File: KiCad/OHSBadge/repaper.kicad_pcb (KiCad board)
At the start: 2 copper layers, 101.6 x 50.8 mm, 59 parts, among them J1 HEADER1X10MS2.54, J2 HEADER1X10MS2.54, J4 ZIF-40-0.5, P1 PCB, Q1 AP2305, Q2 2N7002KW, Q3 BSS84W, Q4 2N7002KW, Q5 2N7002KW, Q6 2N7002KW, Q7 BSS84W, SW1 SEL, SW2 UP, SW3 DOWN, U1 MCP9700AT-E/TT, U3 TPS77030, U4 TXS0108

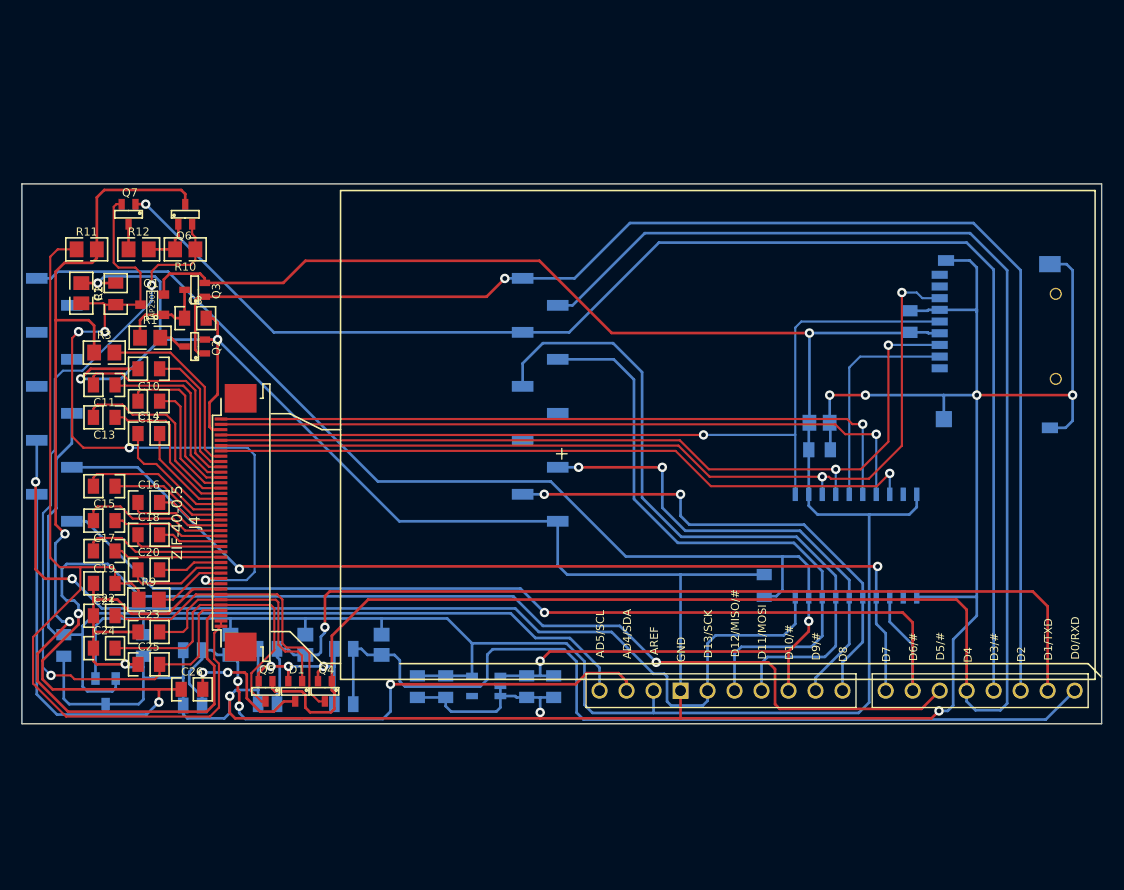
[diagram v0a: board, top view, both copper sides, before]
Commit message: OHSBadge : added 328P, and full Arduino shield. See Board outline for lanyard looping option.
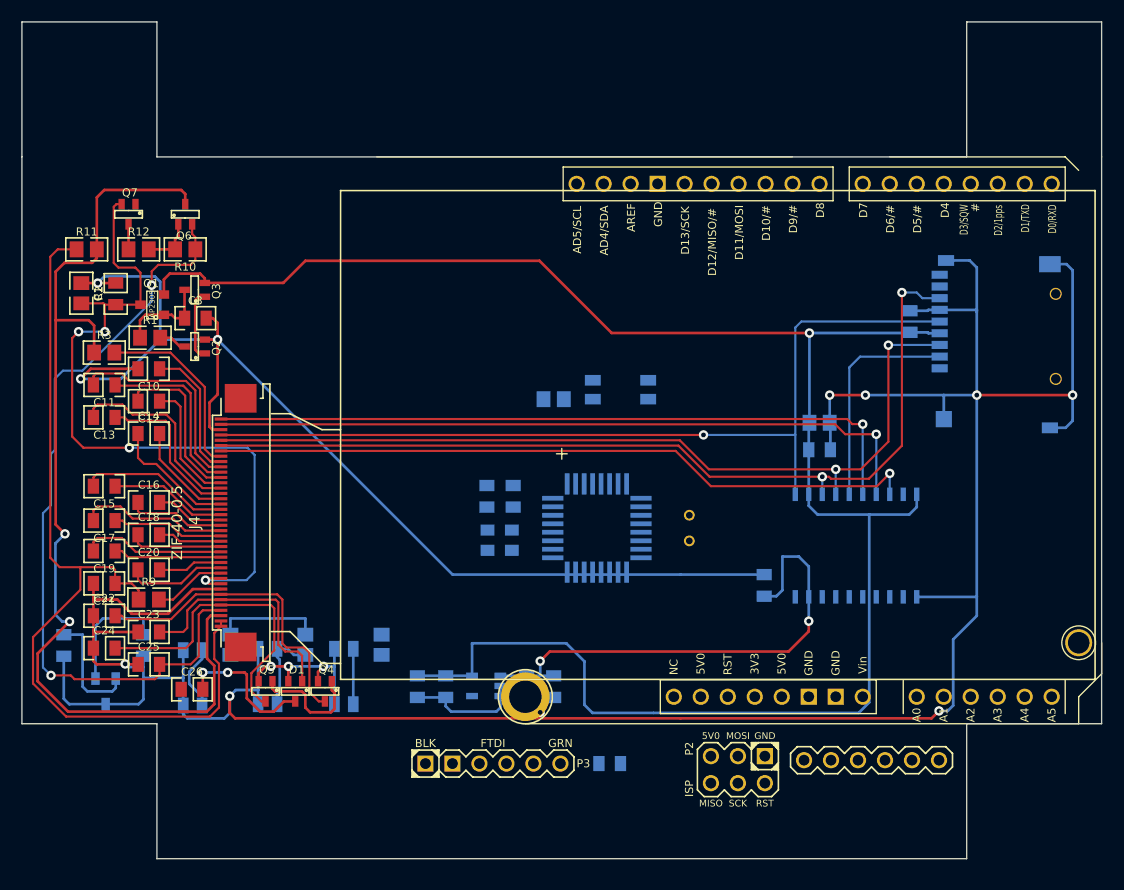
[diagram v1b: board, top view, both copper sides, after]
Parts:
- removed J1, J2: HEADER1X10MS2.54, Sck-10-F-SMT
- added B1: I/O, I/O, F.Cu at (88.2, 84.4)
- added B2: I/O, I/O, F.Cu at (88.2, 82.0)
- added C31: 0.1u,16V, c_0805, B.Cu at (80.7, 105.3)
- added C6: 22pF, c_0805, B.Cu at (71.6, 80.2)
- added C9: 22pF, c_0805, B.Cu at (69.2, 80.2)
- added P2: ISP, Header_ISP, F.Cu at (92.8, 105.9)
- added P3: FTDI, Header_FTDI, F.Cu at (69.7, 105.3)
- added P4: C3SB, Header_6x1, F.Cu at (105.3, 105.0)
- added R7: 10k, r_0805, B.Cu at (75.4, 71.1)
- added SW4: RST, SW_SMD, B.Cu at (81.7, 70.2)
- added U2: ATMEGA328-AU-ND, TQFP32, B.Cu at (79.5, 83.2)
- added X1: CRYSTAL_16MHz, Xtal_SMD2, B.Cu at (70.4, 84.3)
- SHIELD1: footprint ARDUINO_BUCKLER -> ARDUINO_SHIELD_2_040pins
- moved SHIELD1 65.9 mm to (58.8, 101.6)
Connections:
- R4 pad 1: /SDA -> N-0000034
- R4 pad 2: +3.3V -> /VCC5V
- R5 pad 1: /TXD -> N-0000035
- R5 pad 2: +3.3V -> /VCC5V
- R6 pad 1: /RXD -> N-0000036
- R6 pad 2: +3.3V -> /VCC5V
- SHIELD1 pad 10: /VCC5V -> (no net)
- SHIELD1 pad 2: /PANEL_ON -> (no net)
- SHIELD1 pad 3: /BORDER_CONTROL -> (no net)
- SHIELD1 pad 4: /DISCHARGE -> (no net)
- SHIELD1 pad 5: /PWM -> (no net)
- SHIELD1 pad 6: //RESET -> (no net)
- SHIELD1 pad 7: /BUSY -> (no net)
- SHIELD1 pad 8: //EPD_CS -> (no net)
- SHIELD1 pad 9: /FLASH_CS -> (no net)
- SHIELD1 pad AD4: /SDA -> /SCL
- SHIELD1 pad AD5: /TEMPERATURE -> /SCL
- SW1 pad 1: /SDA -> N-0000036
- SW2 pad 1: /TXD -> N-0000035
- SW3 pad 1: /RXD -> N-0000034
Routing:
- net /DISCHARGE: track 177.2 -> 11.0 mm
- net /PWM: track 150.2 -> 0.00 mm, vias 3 -> 0
- net /BORDER_CONTROL: track 129.9 -> 0.00 mm, vias 1 -> 0
- net /PANEL_ON: track 127.8 -> 6.74 mm, vias 1 -> 0
- net /SPI_CLK: track 99.2 -> 0.00 mm, vias 2 -> 0
- net //RESET: track 99.2 -> 0.00 mm, vias 1 -> 0
- net /TXD: track 92.0 -> 0.00 mm, vias 1 -> 0
- net /BUSY: track 92.0 -> 0.00 mm, vias 2 -> 0
- net /RXD: track 85.2 -> 0.00 mm
- net /TEMPERATURE: track 88.0 -> 11.0 mm
- net /VCC5V: track 132.1 -> 57.0 mm
- net /SPI_MOSI: track 65.3 -> 0.00 mm
- net /SPI_MISO: track 58.3 -> 0.00 mm
- net /SDA: track 56.0 -> 0.00 mm, vias 3 -> 0
- net //EPD_CS: track 47.6 -> 0.00 mm, vias 2 -> 0
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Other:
- board size 101.6 x 50.8 mm -> 101.6 x 78.7 mm

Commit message: OHSBadge, work in progress
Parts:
- added H1: I/O, vite_3mm, F.Cu at (31.8, 41.9)
- added H2: I/O, vite_3mm, F.Cu at (120.7, 41.9)
- P4: footprint Header_6x1 -> pin_strip_4-90
- moved P3 19.0 mm to (50.8, 106.7)
- moved C31 18.5 mm to (62.2, 106.6)
- moved P2 16.6 mm to (76.2, 105.4)
- moved P4 4.09 mm to (101.6, 106.7), turned to 0 degrees
- moved P1 1.27 mm to (76.2, 74.9)
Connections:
- SHIELD1 pad AD4: /SCL -> /SDA

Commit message: OHSBadge working on board layout.
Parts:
- added G***: LOGO, LOGO, F.Cu at (32.3, 56.6)
- added G***: LOGO, OSHW_6mm, F.Cu at (98.0, 110.2)
- added G***: LOGO, seeed_LOGO, F.Cu at (118.9, 63.9)
- added G1: Logo-WL3, Logo-WL3, F.Cu at (26.1, 93.6)
- C1, C10, C11, C12, C13, C14, C15, C16, C17, C18, C19, C20, C21, C22, C23, C24, C25, C26, C3, D1, P2, P3, P4, Q1, Q2, Q3, Q4, Q5, Q6, Q7, R1, R10, R11, R12, R2, R3, R9: moved to B.Cu
- J4: footprint ZIF-40-0.5 -> ZIF-40-0.5-M
- SW1: value SEL -> UP; moved to F.Cu
- SW2: value UP -> SEL; moved to F.Cu
- SW3, SW4: moved to F.Cu
- moved C8 64.1 mm to (89.2, 71.5), turned to 180 degrees
- moved U1 60.9 mm to (89.4, 74.9), turned to 90 degrees
- moved C7 54.7 mm to (89.2, 78.4), turned to 0 degrees
- moved R4 47.8 mm to (91.4, 105.7), turned to 90 degrees
- moved SW4 47.8 mm to (109.2, 109.2), turned to 90 degrees
- moved R7 45.0 mm to (104.1, 105.7), turned to 90 degrees
- moved P2 44.0 mm to (116.8, 88.6), turned to 90 degrees
- moved SW3 33.0 mm to (86.4, 109.2), turned to 90 degrees
- moved P4 32.7 mm to (118.1, 78.5), turned to 270 degrees
- moved R5 31.4 mm to (81.3, 105.7), turned to 90 degrees
- moved SW2 30.2 mm to (76.2, 109.2), turned to 90 degrees
- moved SW1 27.3 mm to (66.0, 109.2), turned to 90 degrees
- moved R3 21.6 mm to (54.7, 66.6), turned to 180 degrees
- moved C11 21.6 mm to (54.7, 69.7), turned to 0 degrees
- moved C13 21.6 mm to (54.7, 72.8), turned to 0 degrees
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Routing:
- net GND: track 394.1 -> 0.00 mm, vias 14 -> 0
- net +3.3V: track 187.4 -> 0.00 mm, vias 1 -> 0
- net /BORDER: track 95.5 -> 0.00 mm, vias 2 -> 0
- net /SPI_MISO_COG: track 86.5 -> 0.00 mm, vias 2 -> 0
- net /SPI_CLK_COG: track 83.6 -> 0.00 mm, vias 1 -> 0
- net /VCOM: track 82.8 -> 0.00 mm
- net /SPI_MOSI_COG: track 81.3 -> 0.00 mm, vias 2 -> 0
- net /VDL: track 73.4 -> 0.00 mm, vias 2 -> 0
- net /VCC_T: track 69.8 -> 0.00 mm, vias 4 -> 0
- net /BUSY_COG: track 67.7 -> 0.00 mm, vias 1 -> 0
- net /EPD_CS_COG: track 67.2 -> 0.00 mm, vias 1 -> 0
- net /RESET_COG: track 66.8 -> 0.00 mm, vias 1 -> 0
- net /VCC5V: track 57.0 -> 0.00 mm, vias 2 -> 0
- net /VGH: track 29.6 -> 0.00 mm
- net /VDH: track 28.8 -> 0.00 mm
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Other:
- outline, holes or cut-outs redrawn
- board text added: "SLOT FOR CABLE"

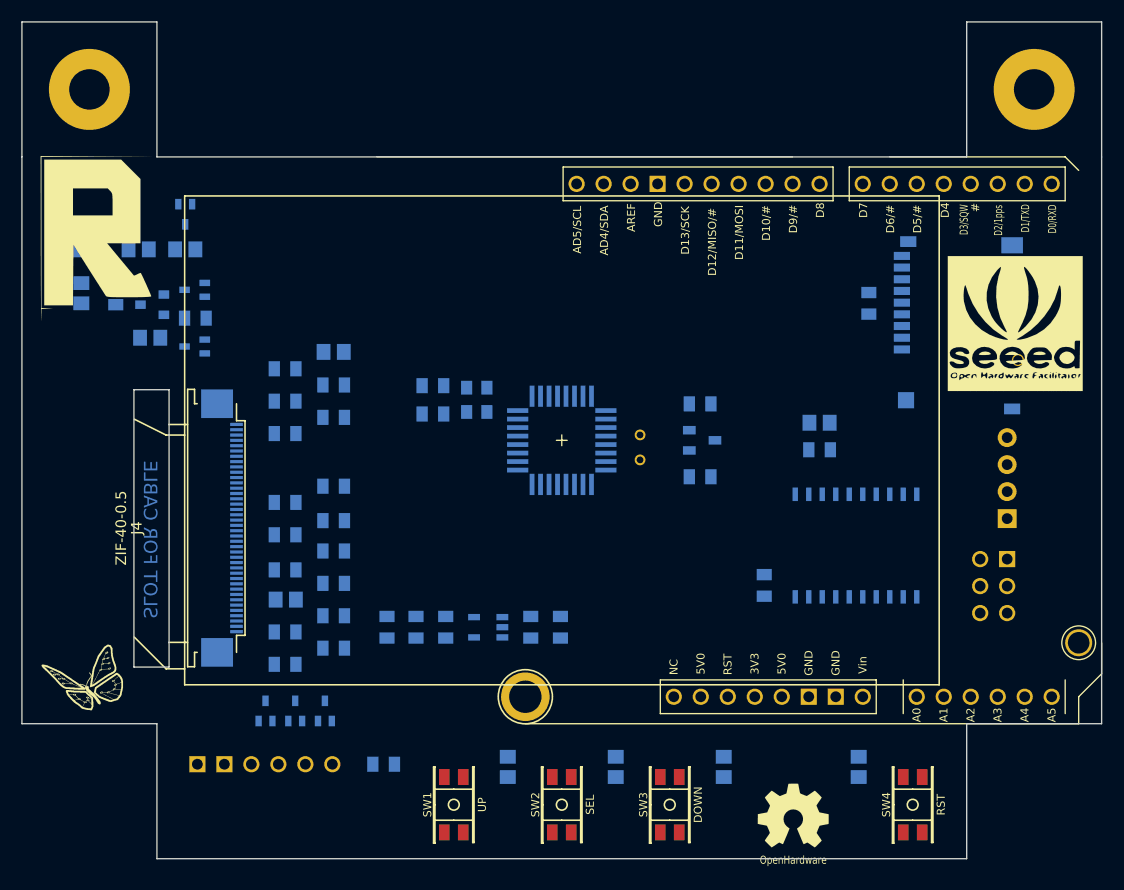
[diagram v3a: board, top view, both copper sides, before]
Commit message: OHSBadge - modified some of the sponsor logos
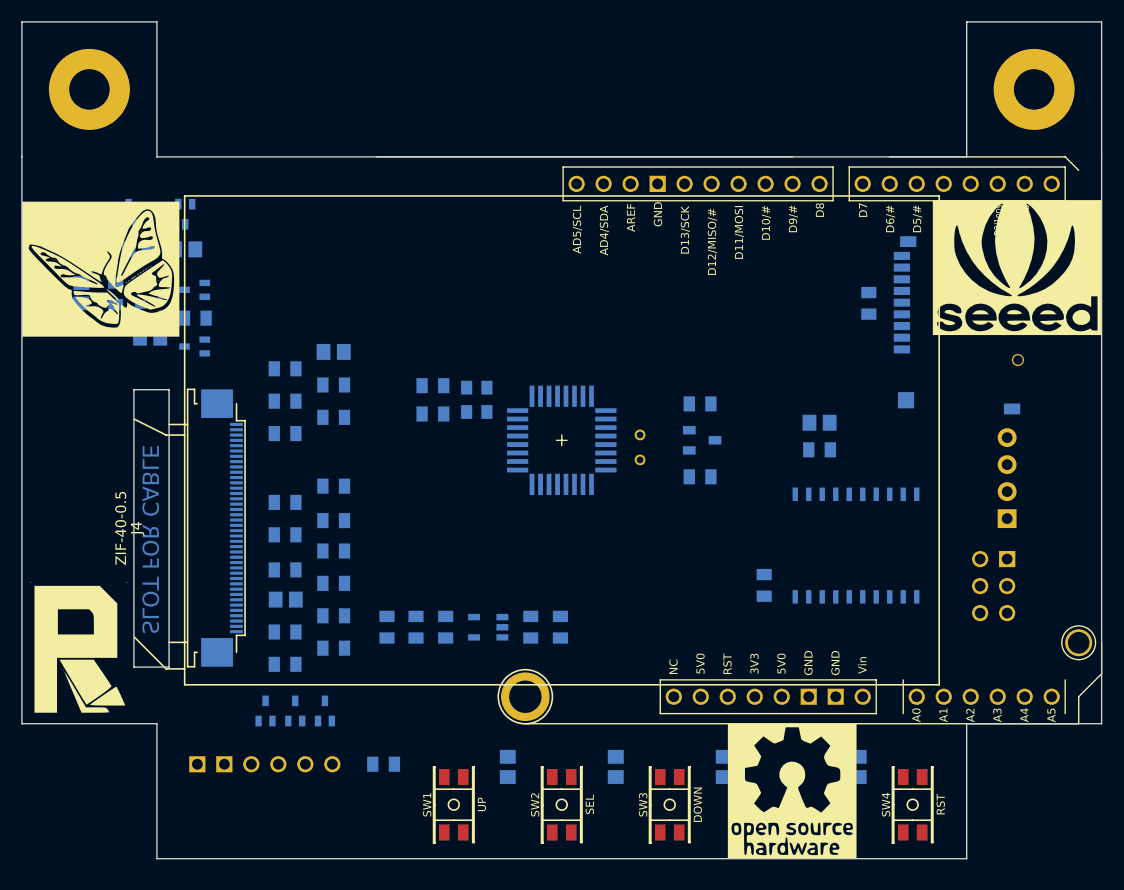
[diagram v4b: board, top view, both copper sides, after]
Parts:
- removed the G*** at (32.3, 56.6)
- removed the G*** at (98.0, 110.2)
- removed the G*** at (118.9, 63.9)
- removed G1: Logo-WL3, Logo-WL3
- added G***: osh_logo, osh_logo, F.Cu at (97.8, 108.0)
- added G***: repaper_logo, repaper_logo, F.Cu at (30.7, 94.6)
- added G***: seeed_logo, seeed_logo, F.Cu at (119.1, 58.7)
- added G***: wyo_logo, wyo_logo, F.Cu at (32.8, 58.8)

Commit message: OHSBadge, Schematic update, added coin batt, JST connector, 3V3 selector.
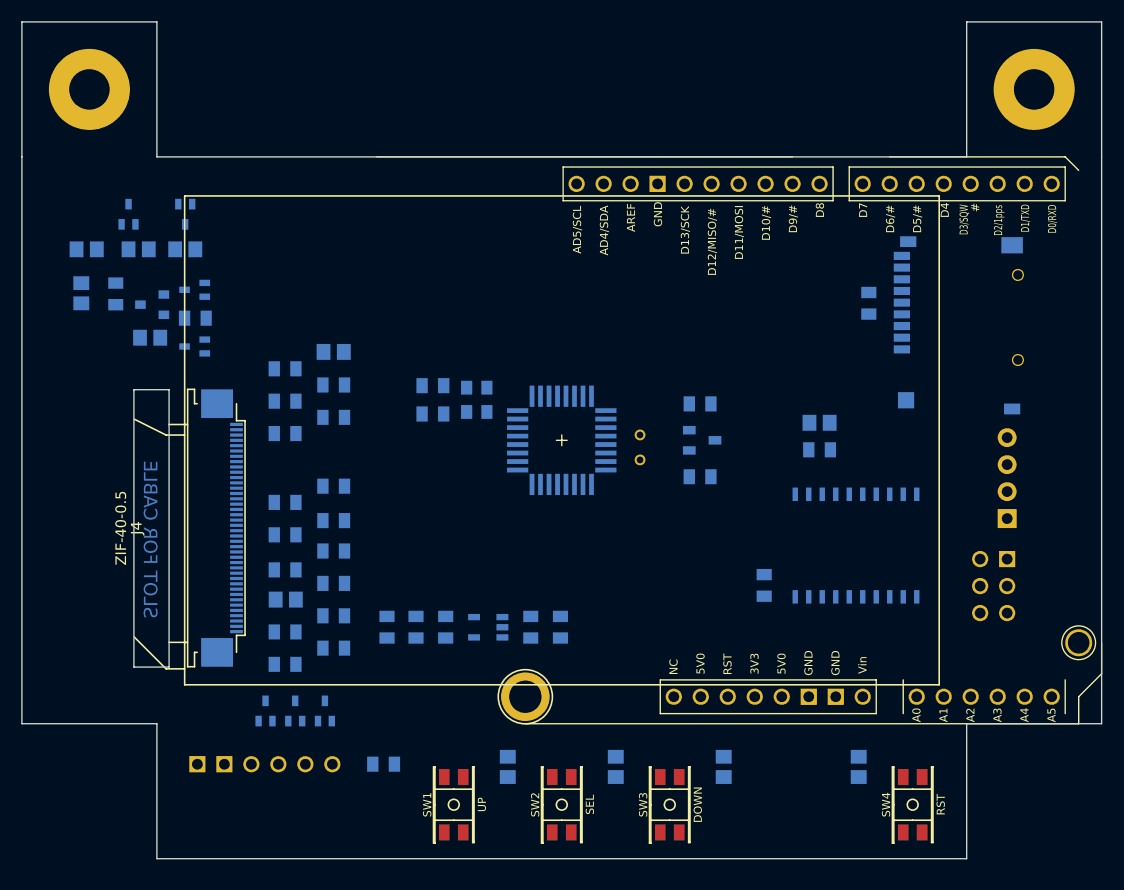
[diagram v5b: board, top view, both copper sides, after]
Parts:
- removed G***: osh_logo, osh_logo
- removed G***: repaper_logo, repaper_logo
- removed G***: seeed_logo, seeed_logo
- removed G***: wyo_logo, wyo_logo

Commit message: OHSBadge : Moved old files to archive folder. ISP header is 3V3. No SPI connection to shield. Spare uC pins on breakouts, and also via level shifter. SMD coin battery retainer added. Rounded board corners.
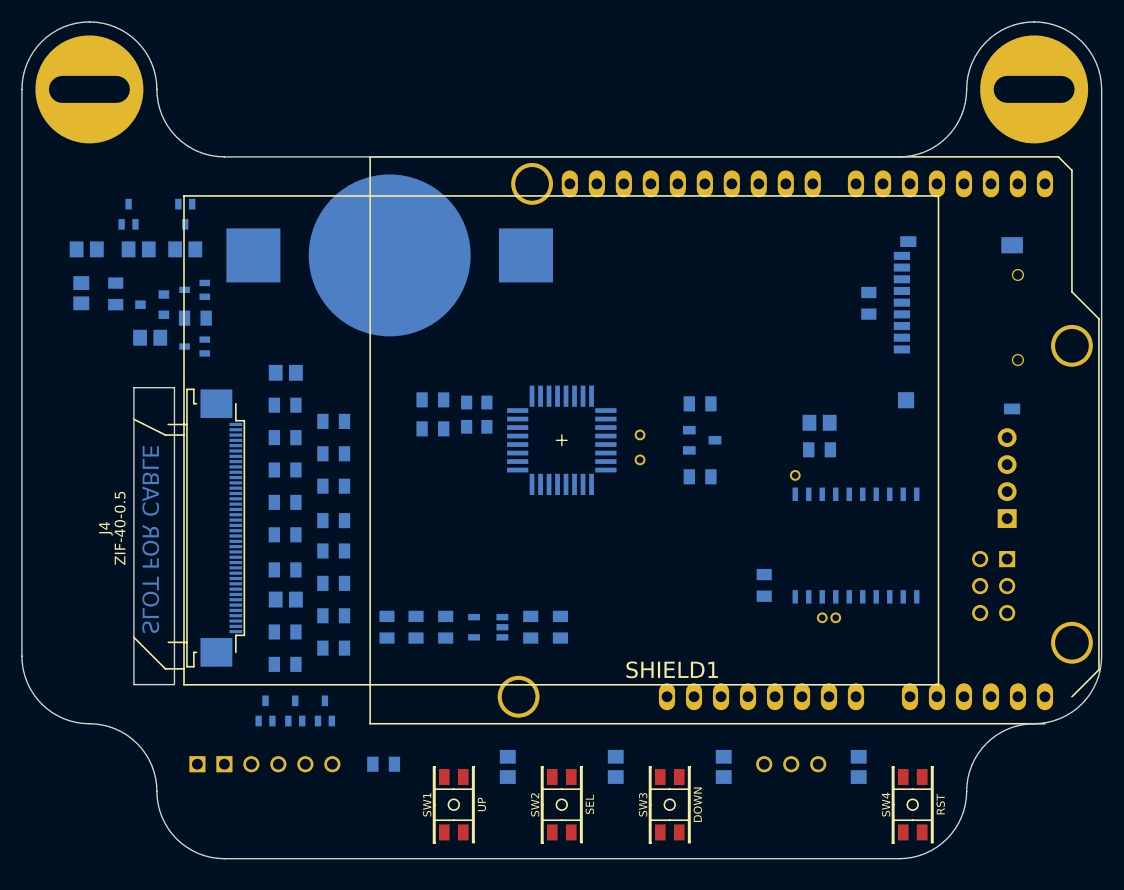
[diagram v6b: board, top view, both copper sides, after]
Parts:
- added B3: I/O, I/O, F.Cu at (98.2, 78.2)
- added B4: I/O, I/O, F.Cu at (100.7, 91.6)
- added B5: I/O, I/O, F.Cu at (102.0, 91.6)
- added BT1: Batt_Clip, CR2032_SMD, B.Cu at (60.0, 57.5)
- added P6: 3V3_SEL, Header_A_REF, B.Cu at (97.8, 105.4)
- SHIELD1: footprint ARDUINO_SHIELD_2_040pins -> ARDUINO_SHIELD_040pins
- U3: value TPS77030 -> MCP1700T-33
- X1: value CRYSTAL_16MHz -> CRYSTAL_8MHz
- moved R3 4.92 mm to (50.2, 68.6)
- moved C10 3.43 mm to (50.2, 71.6), turned to 180 degrees
- moved C11 3.43 mm to (54.7, 73.2), turned to 180 degrees
- moved C12 3.43 mm to (50.2, 74.7), turned to 180 degrees
- moved C13 3.43 mm to (54.7, 76.2), turned to 180 degrees
- moved C14 3.43 mm to (50.2, 77.7), turned to 180 degrees
- moved C6 1.40 mm to (64.1, 73.9)
- moved X1 1.40 mm to (68.2, 72.5)
- moved C9 1.33 mm to (64.1, 71.1)
- moved SHIELD1 0.64 mm to (58.2, 101.6)
- moved J4 0.06 mm to (29.4, 83.2)
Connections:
- net N-0000017 renamed /DTR
- net N-0000035 renamed /UP
- B1 pad 1: /AD6 -> /AD6_3V3
- B2 pad 1: /AD7 -> /AD7_3V3
- C27 pad 1: +3.3V -> GND
- C27 pad 2: GND -> /3V3
- C28 pad 1: +3.3V -> N-0000050
- C29 pad 1: /VCC5V -> /3V3
- C4 pad 1: +3.3V -> /3V3
- C5 pad 1: +3.3V -> /3V3
- C7 pad 2: +3.3V -> /3V3
- H1 pad 1: (no net) -> N-0000050
- H2 pad 1: (no net) -> GND
- J4 pad 1: /EPD_CS_COG -> //EPD_CS_3V3
- J4 pad 2: /BUSY_COG -> /BUSY_3V3
- J4 pad 4: /SPI_CLK_COG -> /SPI_CLK_3V3
- J4 pad 5: /SPI_MOSI_COG -> /SPI_MOSI_3V3
- J4 pad 6: /SPI_MISO_COG -> /SPI_MISO_3V3
- J4 pad 7: /RESET_COG -> //RESET_3V3
- P4 pad 1: /SDA -> /VCC5V
- P4 pad 3: /VCC5V -> /SDA
- Q1 pad 2: +3.3V -> /3V3
- Q3 pad 2: +3.3V -> /3V3
- R16 pad 2: +3.3V -> /3V3
- R4 pad 1: N-0000034 (its old number) -> /DOWN
- R4 pad 2: /VCC5V -> /3V3
- R5 pad 1: N-0000033 (its old number) -> /SEL
- R5 pad 2: /VCC5V -> /3V3
- R6 pad 2: /VCC5V -> /3V3
- R7 pad 1: /RST -> /RST_3V3
- R7 pad 2: /VCC5V -> /3V3
- SD1 pad 2: /FLASH_CS_COG -> /FLASH_CS_3V3
- SD1 pad 3: /SPI_MOSI_COG -> /SPI_MOSI_3V3
- SD1 pad 4: +3.3V -> /3V3
- SD1 pad 5: /SPI_CLK_COG -> /SPI_CLK_3V3
- SD1 pad 7: /SPI_MISO_COG -> /SPI_MISO_3V3
- SHIELD1 pad 1: /TXD -> /TXD_3V3
- SHIELD1 pad 10: (no net) -> /SPI_SS
- SHIELD1 pad 3V3: (no net) -> /VCC3V
- SHIELD1 pad AD4: /SDA -> (no net)
- SHIELD1 pad AREF: +3.3V -> /3V3
- SW2 pad 1: N-0000033 (its old number) -> /SEL
- SW3 pad 1: N-0000034 (its old number) -> /DOWN
- SW4 pad 2: /RST -> /RST_3V3
- U1 pad 1: +3.3V -> /3V3
- U2 pad 10: //RESET -> //RESET_3V3
- U2 pad 11: /BUSY -> /BUSY_3V3
- U2 pad 12: //EPD_CS -> //EPD_CS_3V3
- U2 pad 13: /FLASH_CS -> /FLASH_CS_3V3
- U2 pad 14: (no net) -> /SPI_SS_3V3
- U2 pad 15: /SPI_MOSI -> /SPI_MOSI_3V3
- U2 pad 16: /SPI_MISO -> /SPI_MISO_3V3
- U2 pad 17: /SPI_CLK -> /SPI_CLK_3V3
- U2 pad 18: /VCC5V -> /3V3
- U2 pad 19: /AD6 -> /AD6_3V3
- U2 pad 20: +3.3V -> /3V3
- U2 pad 22: /AD7 -> /AD7_3V3
- U2 pad 25: N-0000033 (its old number) -> /SEL
- U2 pad 26: N-0000034 (its old number) -> /DOWN
- U2 pad 27: /SDA -> /SDA_3V3
- U2 pad 28: /SCL -> /SCL_3V3
- U2 pad 29: /RST -> /RST_3V3
- U2 pad 30: /TXD -> /RXD_3V3
- U2 pad 31: /RXD -> /TXD_3V3
- U2 pad 4: /VCC5V -> /3V3
- U2 pad 6: /VCC5V -> /3V3
- U3 pad 1: /VCC5V -> GND
- U3 pad 2: GND -> /VCC5V
- U3 pad 3: GND -> N-0000050
- U3 pad 5: +3.3V -> (no net)
- U4 pad 1: /SPI_CLK_COG -> /SPI_SS_3V3
- U4 pad 10: +3.3V -> /3V3
- U4 pad 12: (no net) -> /RXD
- U4 pad 13: //RESET -> /TXD
- U4 pad 14: /BUSY -> /RST
- U4 pad 15: //EPD_CS -> /SCL
- U4 pad 16: /FLASH_CS -> /SDA
- U4 pad 17: /SPI_MOSI -> /AD6
- U4 pad 18: /SPI_MISO -> /AD7
- U4 pad 2: +3.3V -> /3V3
- U4 pad 20: /SPI_CLK -> /SPI_SS
- U4 pad 3: /SPI_MISO_COG -> /AD7_3V3
- U4 pad 4: /SPI_MOSI_COG -> /AD6_3V3
- U4 pad 5: /FLASH_CS_COG -> /SDA_3V3
- U4 pad 6: /EPD_CS_COG -> /SCL_3V3
- U4 pad 7: /BUSY_COG -> /RST_3V3
- U4 pad 8: /RESET_COG -> /TXD_3V3
- U4 pad 9: (no net) -> /RXD_3V3
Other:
- outline, holes or cut-outs redrawn
